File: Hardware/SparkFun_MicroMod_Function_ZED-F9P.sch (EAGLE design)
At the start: 39 parts, among them J11 MICROMOD_STANDARD, J5 QWIIC_RA, U1 EEPROM, U2 U-BLOX_ZED-F9P

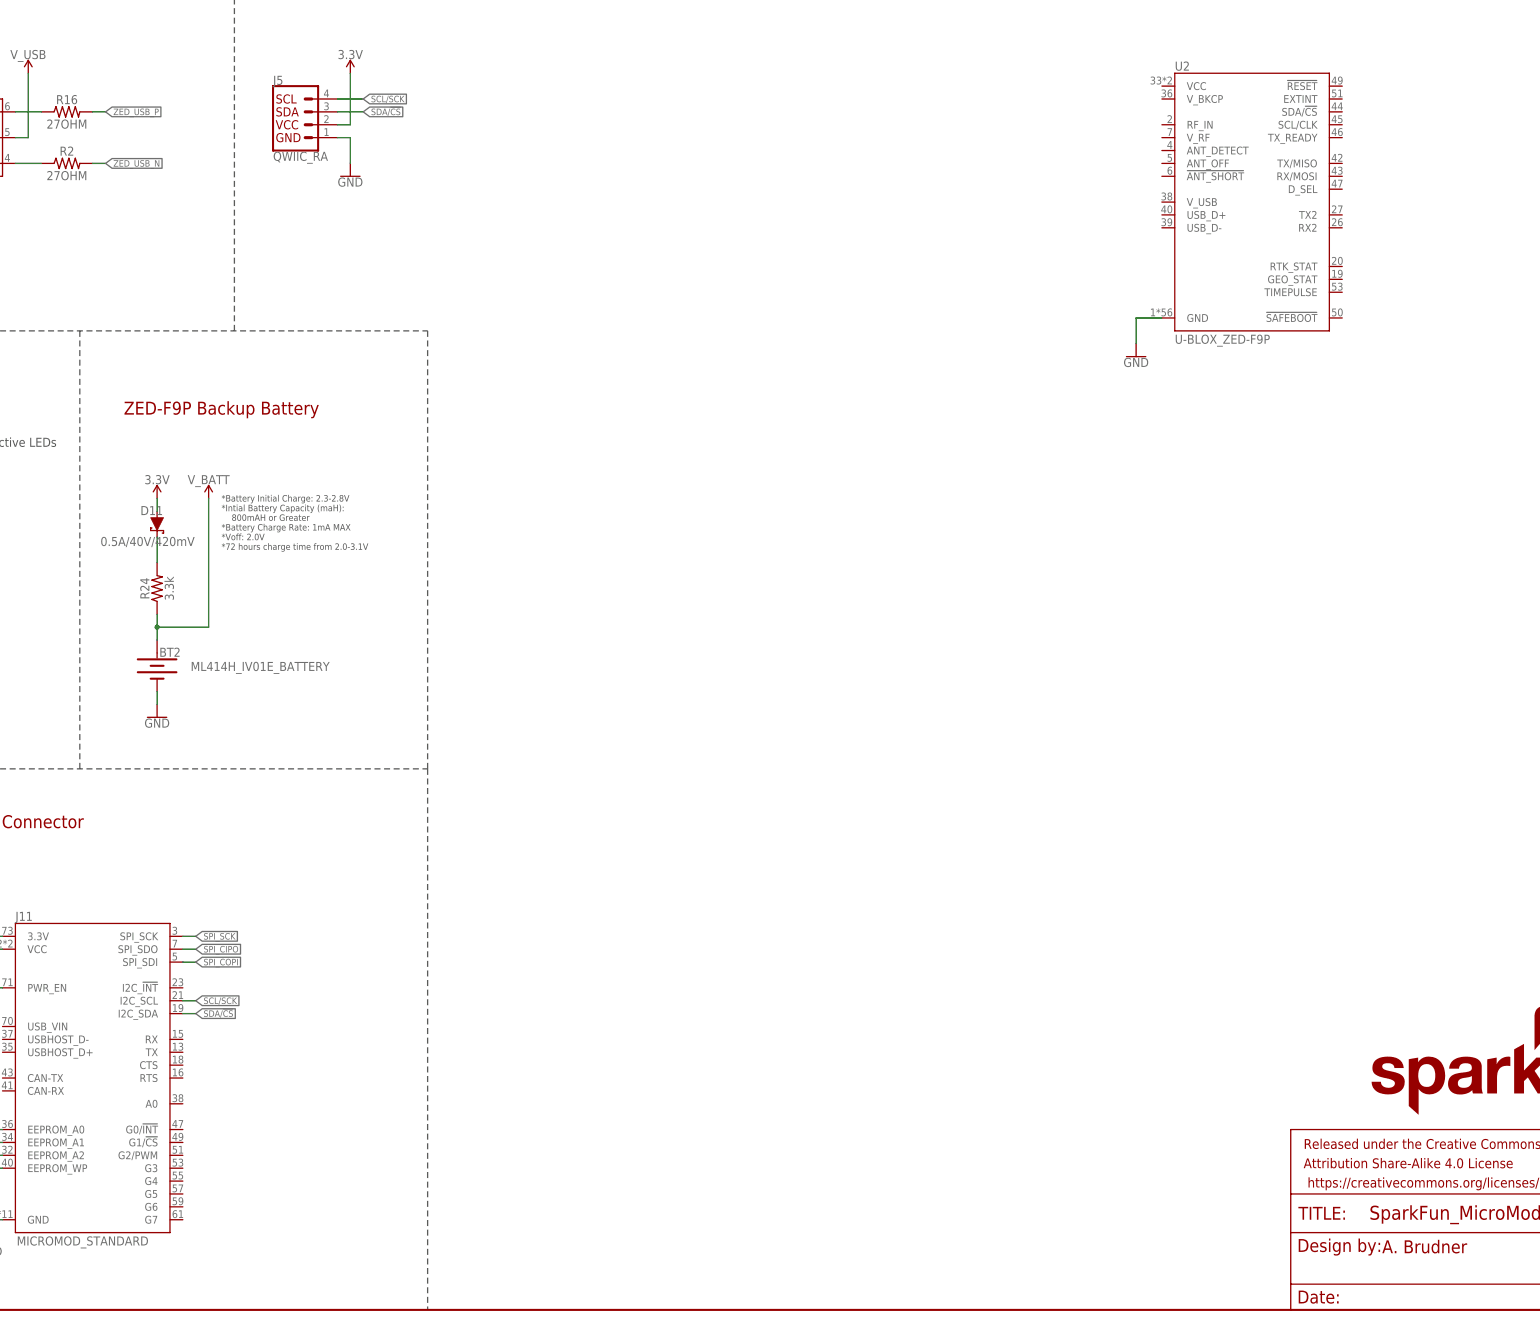
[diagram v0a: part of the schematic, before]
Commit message: Added I2C protection for ZED_F9P
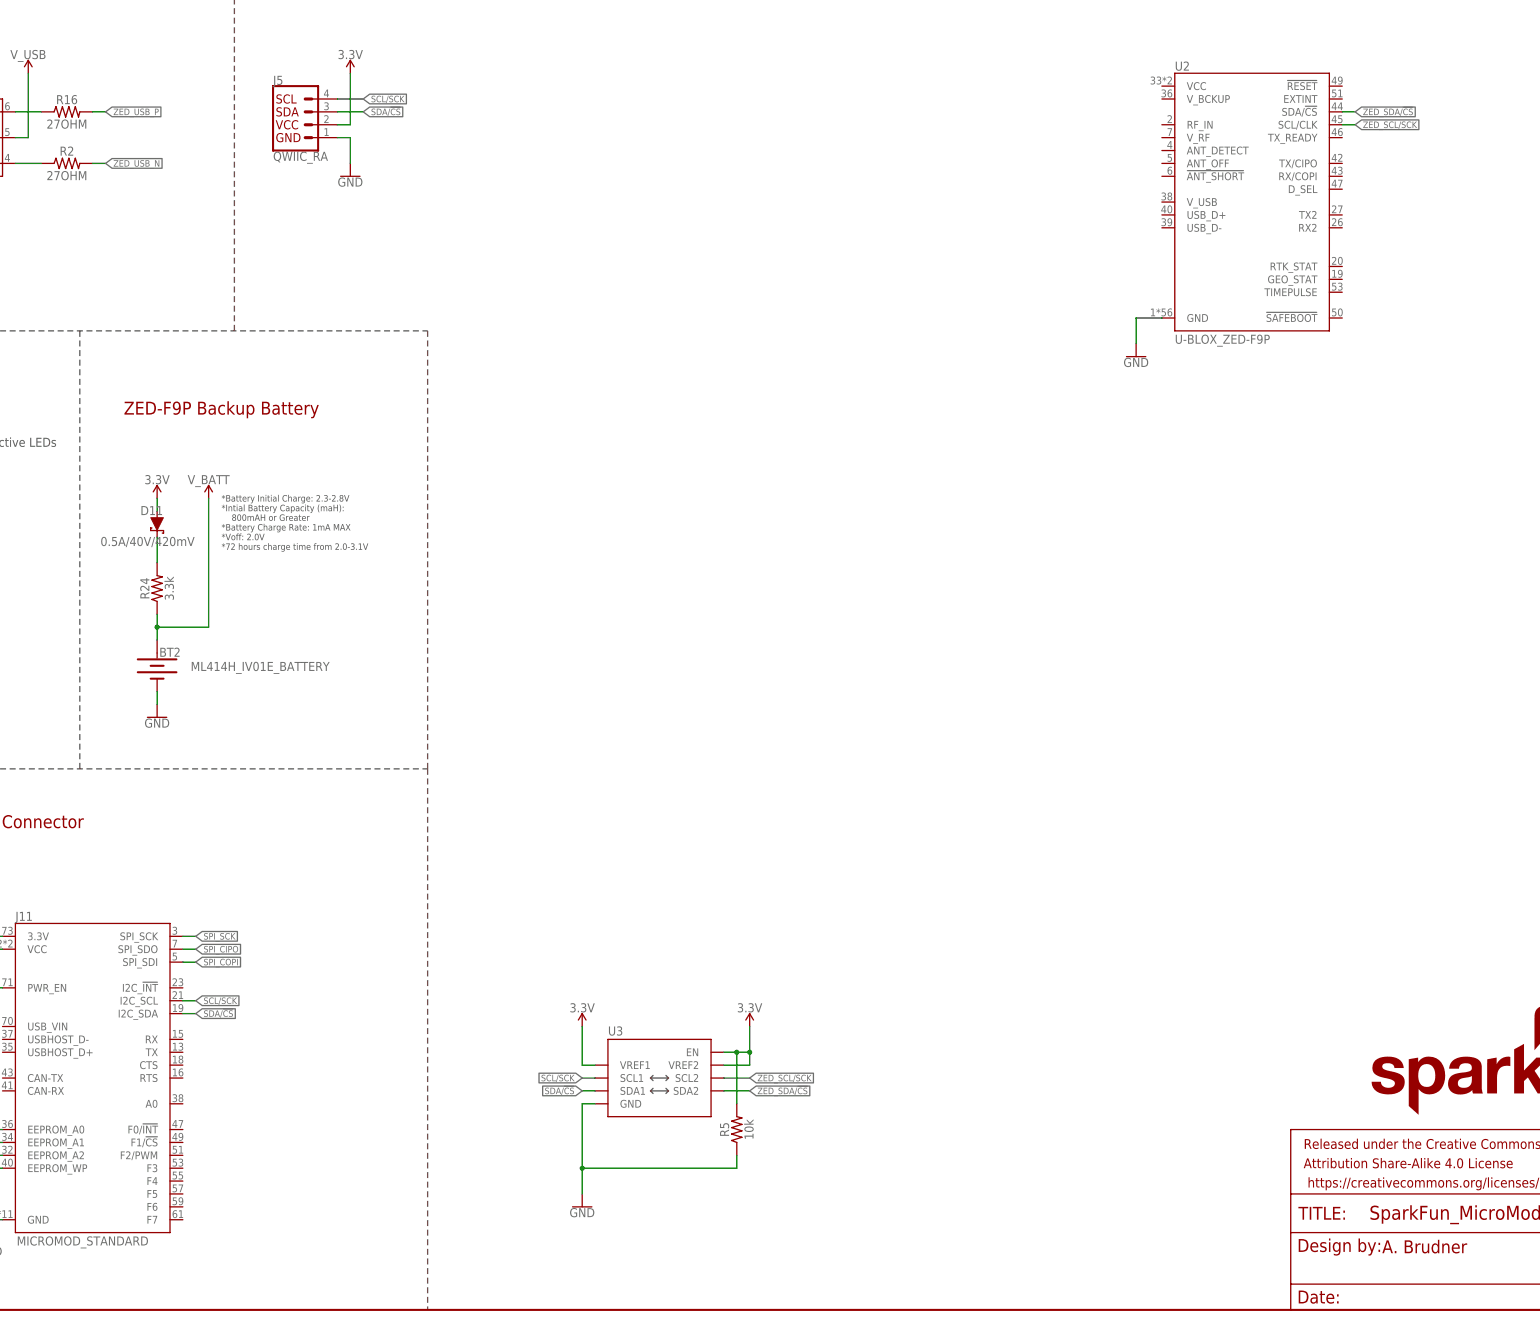
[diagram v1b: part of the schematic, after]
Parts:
- added R5: 10k, SparkFun-Resistors:10KOHM-0603-1/10W-1%
- added U3: (no value), SparkFun-IC-Comms:PCA9306VSSOP_DCU
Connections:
- new net ZED_SCL/SCK: U2.SCL/CLK, U3.SCL2
- new net ZED_SDA/!CS!: U2.SDA/!CS!, U3.SDA2
- net 3.3V: now also R5.2, U3.EN, U3.VREF1, U3.VREF2
- net GND: now also R5.1, U3.GND
- net SCL/SCK: now also U3.SCL1
- net SDA/!CS!: now also U3.SDA1
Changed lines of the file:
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@@
 <part name="GND27" library="SparkFun-PowerSymbols" deviceset="GND" device=""/>
 <part name="SUPPLY11" library="SparkFun-PowerSymbols" deviceset="3.3V" device=""/>
+<part name="U3" library="SparkFun-IC-Comms" deviceset="PCA9306" device="VSSOP_DCU" package3d_urn="urn:adsk.eagle:package:34687508/1"/>
+<part name="GND4" library="SparkFun-PowerSymbols" deviceset="GND" device=""/>
+<part name="SUPPLY10" library="SparkFun-PowerSymbols" deviceset="3.3V" device=""/>
+<part name="SUPPLY12" library="SparkFun-PowerSymbols" deviceset="3.3V" device=""/>
+<part name="R5" library="SparkFun-Resistors" deviceset="10KOHM" device="-0603-1/10W-1%" value="10k"/>
 </parts>
 <sheets>
@@
 <attribute name="VALUE" x="144.78" y="246.634" size="1.778" layer="96" font="vector" align="bottom-center"/>
 </instance>
+<instance part="U3" gate="G$1" x="205.74" y="45.72" smashed="yes">
+<attribute name="NAME" x="195.58" y="54.102" size="1.778" layer="95"/>
+<attribute name="VALUE" x="195.58" y="35.56" size="1.778" layer="96"/>
+</instance>
+<instance part="GND4" gate="1" x="190.5" y="20.32" smashed="yes">
+<attribute name="VALUE" x="190.5" y="20.066" size="1.778" layer="96" font="vector" align="top-center"/>
+</instance>
+<instance part="SUPPLY10" gate="G$1" x="190.5" y="55.88" smashed="yes">
+<attribute name="VALUE" x="190.5" y="58.674" size="1.778" layer="96" align="bottom-center"/>
+</instance>
+<instance part="SUPPLY12" gate="G$1" x="223.52" y="55.88" smashed="yes">
+<attribute name="VALUE" x="223.52" y="58.674" size="1.778" layer="96" align="bottom-center"/>
+</instance>
+<instance part="R5" gate="G$1" x="220.98" y="35.56" smashed="yes" rot="R90">
+<attribute name="NAME" x="219.456" y="35.56" size="1.778" layer="95" font="vector" rot="R90" align="bottom-center"/>
+<attribute name="VALUE" x="222.504" y="35.56" size="1.778" layer="96" font="vector" rot="R90" align="top-center"/>
+</instance>
 </instances>
 <busses>
@@
 <wire x1="142.24" y1="231.14" x2="144.78" y2="231.14" width="0.1524" layer="91"/>
 </segment>
+<segment>
+<pinref part="U3" gate="G$1" pin="GND"/>
+<wire x1="193.04" y1="40.64" x2="190.5" y2="40.64" width="0.1524" layer="91"/>
+<wire x1="190.5" y1="40.64" x2="190.5" y2="27.94" width="0.1524" layer="91"/>
+<pinref part="GND4" gate="1" pin="GND"/>
+<pinref part="R5" gate="G$1" pin="1"/>
+<wire x1="190.5" y1="27.94" x2="190.5" y2="22.86" width="0.1524" layer="91"/>
+<wire x1="190.5" y1="27.94" x2="220.98" y2="27.94" width="0.1524" layer="91"/>
+<wire x1="220.98" y1="27.94" x2="220.98" y2="30.48" width="0.1524" layer="91"/>
+<junction x="190.5" y="27.94"/>
+</segment>
 </net>
 <net name="3.3V" class="0">
@@
 <wire x1="142.24" y1="233.68" x2="144.78" y2="233.68" width="0.1524" layer="91"/>
 <pinref part="SUPPLY11" gate="G$1" pin="3.3V"/>
+</segment>
+<segment>
+<pinref part="U3" gate="G$1" pin="VREF1"/>
+<wire x1="193.04" y1="48.26" x2="190.5" y2="48.26" width="0.1524" layer="91"/>
+<wire x1="190.5" y1="48.26" x2="190.5" y2="55.88" width="0.1524" layer="91"/>
+<pinref part="SUPPLY10" gate="G$1" pin="3.3V"/>
+</segment>
+<segment>
+<pinref part="U3" gate="G$1" pin="VREF2"/>
+<wire x1="218.44" y1="48.26" x2="223.52" y2="48.26" width="0.1524" layer="91"/>
+<wire x1="223.52" y1="48.26" x2="223.52" y2="50.8" width="0.1524" layer="91"/>
+<pinref part="U3" gate="G$1" pin="EN"/>
+<wire x1="223.52" y1="50.8" x2="223.52" y2="55.88" width="0.1524" layer="91"/>
+<wire x1="218.44" y1="50.8" x2="220.98" y2="50.8" width="0.1524" layer="91"/>
+<junction x="223.52" y="50.8"/>
+<pinref part="SUPPLY12" gate="G$1" pin="3.3V"/>
+<pinref part="R5" gate="G$1" pin="2"/>
+<wire x1="220.98" y1="50.8" x2="223.52" y2="50.8" width="0.1524" layer="91"/>
+<wire x1="220.98" y1="40.64" x2="220.98" y2="50.8" width="0.1524" layer="91"/>
+<junction x="220.98" y="50.8"/>
 </segment>
 </net>
@@
 <label x="114.3" y="60.96" size="1.27" layer="95" xref="yes"/>
 </segment>
+<segment>
+<pinref part="U3" gate="G$1" pin="SCL1"/>
+<wire x1="193.04" y1="45.72" x2="190.5" y2="45.72" width="0.1524" layer="91"/>
+<label x="190.5" y="45.72" size="1.27" layer="95" rot="R180" xref="yes"/>
+</segment>
 </net>
 <net name="SDA/!CS!" class="0">
@@
 <label x="114.3" y="58.42" size="1.27" layer="95" xref="yes"/>
 </segment>
-</net>
+<segment>
+<pinref part="U3" gate="G$1" pin="SDA1"/>
+<wire x1="193.04" y1="43.18" x2="190.5" y2="43.18" width="0.1524" layer="91"/>
+<label x="190.5" y="43.18" size="1.27" layer="95" rot="R180" xref="yes"/>
+</segment>
+</net>
+<net name="ZED_SCL/SCK" class="0">
+<segment>
+<pinref part="U3" gate="G$1" pin="SCL2"/>
+<wire x1="218.44" y1="45.72" x2="223.52" y2="45.72" width="0.1524" layer="91"/>
+<label x="223.52" y="45.72" size="1.27" layer="95" xref="yes"/>
+</segment>
+<segment>
+<pinref part="U2" gate="U1" pin="SCL/CLK"/>
+<wire x1="340.36" y1="233.68" x2="342.9" y2="233.68" width="0.1524" layer="91"/>
+<label x="342.9" y="233.68" size="1.27" layer="95" xref="yes"/>
+</segment>
+</net>
+<net name="ZED_SDA/!CS!" class="0">
+<segment>
+<pinref part="U3" gate="G$1" pin="SDA2"/>
+<wire x1="218.44" y1="43.18" x2="223.52" y2="43.18" width="0.1524" layer="91"/>
+<label x="223.52" y="43.18" size="1.27" layer="95" xref="yes"/>
+</segment>
+<segment>
+<pinref part="U2" gate="U1" pin="SDA/!CS!"/>
+<wire x1="340.36" y1="236.22" x2="342.9" y2="236.22" width="0.1524" layer="91"/>
+<label x="342.9" y="236.22" size="1.27" layer="95" xref="yes"/>
+</segment>
+</net>

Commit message: Created local library. Added ZED-F9P to sch.
Created Local library.
Added inverter to lib.
Added octal buffer to lib.
Added modified ZED-F9P to lib.
Added ZED-F9P to sch.
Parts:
- removed U2: U-BLOX_ZED-F9P, SparkFun-GPS:U-BLOX_ZED-F9P
- removed U3: (no value), SparkFun-IC-Comms:PCA9306VSSOP_DCU
- renumbered BT2 to $1_0_$_2022-03-17_14-46-28, C4 to $1_1_$_2022-03-17_14-46-28, D10 to $1_6_$_2022-03-17_14-46-28, D11 to $1_8_$_2022-03-17_14-46-28, D2 to $1_3_$_2022-03-17_14-46-28, D3 to $1_2_$_2022-03-17_14-46-28, D4 to $1_7_$_2022-03-17_14-46-28, D8 to $1_4_$_2022-03-17_14-46-28, D9 to $1_5_$_2022-03-17_14-46-28, FD1 to $1_9_$_2022-03-17_14-46-28, FD2 to $1_11_$_2022-03-17_14-46-28, FD3 to $1_12_$_2022-03-17_14-46-28, FD4 to $1_10_$_2022-03-17_14-46-28, FRAME1 to $1_13_$_2022-03-17_14-46-28
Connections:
- removed net ZED_SCL/SCK: U2.SCL/CLK, U3.SCL2
- removed net ZED_SDA/!CS!: U2.SDA/!CS!, U3.SDA2
- net 3.3V: no longer U3.EN, U3.VREF1, U3.VREF2
- net GND: no longer U2.GND, U3.GND
- net SCL/SCK: no longer U3.SCL1
- net SDA/!CS!: no longer U3.SDA1

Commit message: Filled out octal buffers, labeled nets. Modified inverter sch symbol.
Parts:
- removed $1_1_$_2022-03-17_14-46-28: 0.1uF, SparkFun-Capacitors:0.1UF-0603-25V-(+80/-20%)
- removed J11: MICROMOD_STANDARD, SparkFun-MicroMod-Function:MICROMOD_STANDARD
- removed J5: QWIIC_RA, SparkFun-Connectors:QWIIC_CONNECTORJS-1MM
- removed R19, R21: 1k, SparkFun-Resistors:1KOHM-0603-1/10W-1%
- removed R22: 10k, SparkFun-Resistors:10KOHM-0603-1/10W-1%
- removed RTK: JUMPER-SMT_2_NC_TRACE_SILK, SparkFun-Jumpers:JUMPER-SMT_2_NC_TRACE_SILK
- added C1: 10pF, SparkFun-Capacitors:10PF-0603-50V-5%
- added C2: 0.1uF, SparkFun-Capacitors:0.1UF-0603-25V-(+80/-20%)
- added J1: (no value), SparkFun-Connectors:USB_C_2-LAYER_PADS
- added J2: MICROMOD_STANDARD, SparkFun-MicroMod-Function:MICROMOD_STANDARD
- added JP1: JUMPER-SMT_2_NO_SILK, SparkFun-Jumpers:JUMPER-SMT_2_NO_SILK
- added JP7: NC, SparkFun-Jumpers:JUMPER-SMT_2_NC_TRACE_SILK
- added R10, R9: 27OHM, SparkFun-Resistors:27OHM
- added R12: 220k, SparkFun-Resistors:220KOHM-0603-1/10W-1%
- added R13, R14, R15: 1.5k, SparkFun-Resistors:1.5KOHM-0603-1/10W-1%
- added R17: 10k, SparkFun-Resistors:10KOHM-0603-1/10W-1%
- added R8: 5.1k, SparkFun-Resistors:5.1KOHM5.1KOHM-0603-1/10W-1%
- added U2: PCA9306DCUR, MicroMod_Function_GNSS_ublox_ZED-F9P:PCA9306DCUR
- added U3: U-BLOX_ZED-F9P, MicroMod_Function_GNSS_ublox_ZED-F9P:U-BLOX_ZED-F9P
- added U4, U5: 74LVC541ABQ, MicroMod_Function_GNSS_ublox_ZED-F9P:74LVC541ABQ
- added U6: SN74AUP1T04DCK, MicroMod_Function_GNSS_ublox_ZED-F9P:SN74AUP1T04DCK
- J3: value (none) -> QWIIC_RA; device SparkFun-Connectors:USB_C_2-LAYER_PADS -> SparkFun-Connectors:QWIIC_CONNECTORJS-1MM
- JP5: value JUMPER-SMT_2_NO_SILK -> JUMPER-SMT_2_NC_TRACE_SILK; device SparkFun-Jumpers:JUMPER-SMT_2_NO_SILK -> SparkFun-Jumpers:JUMPER-SMT_2_NC_TRACE_SILK
- R1: value 5.1k -> 10k; device SparkFun-Resistors:5.1KOHM5.1KOHM-0603-1/10W-1% -> SparkFun-Resistors:10KOHM-0603-1/10W-1%
- R16: value 27OHM -> 1.5k; device SparkFun-Resistors:27OHM -> SparkFun-Resistors:1.5KOHM-0603-1/10W-1%
- R2: value 27OHM -> 5.1k; device SparkFun-Resistors:27OHM -> SparkFun-Resistors:5.1KOHM5.1KOHM-0603-1/10W-1%
- R5: value 10k -> 1k; device SparkFun-Resistors:10KOHM-0603-1/10W-1% -> SparkFun-Resistors:1KOHM-0603-1/10W-1%
- R7: value 5.1k -> 1k; device SparkFun-Resistors:5.1KOHM5.1KOHM-0603-1/10W-1% -> SparkFun-Resistors:1KOHM-0603-1/10W-1%
- renumbered $1_0_$_2022-03-17_14-46-28 to BT1, $1_10_$_2022-03-17_14-46-28 to FD2, $1_11_$_2022-03-17_14-46-28 to FD3, $1_12_$_2022-03-17_14-46-28 to FD4, $1_13_$_2022-03-17_14-46-28 to FRAME1, $1_2_$_2022-03-17_14-46-28 to D1, $1_3_$_2022-03-17_14-46-28 to D2, $1_4_$_2022-03-17_14-46-28 to D3, $1_5_$_2022-03-17_14-46-28 to D4, $1_6_$_2022-03-17_14-46-28 to D5, $1_7_$_2022-03-17_14-46-28 to D6, $1_8_$_2022-03-17_14-46-28 to D7, $1_9_$_2022-03-17_14-46-28 to FD1, 3V3 to JP3, GEOF to JP6, PPS to JP4, R20 to R6, R24 to R11, VIN to JP2
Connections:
- removed net SPI_CIPO: J11.SPI_SDO
- removed net SPI_COPI: J11.SPI_SDI
- removed net SPI_SCK: J11.SPI_SCK
- new net !RESET!: U4.A2
- new net !SAFEBOOT!: U4.A3
- new net !SHORT!: U4.A6
- new net ANT_DETECT: U4.A5
- new net ANT_OFF: U5.Y0
- new net EXTINT: U4.A4
- new net IO_!OE!: U4.!OE1!, U4.!OE2!, U5.!OE1!, U5.!OE2!, U6.Y
- new net N$12: C1.1, R12.1, U2.EN, U2.VREF2
- new net N$13: C2.1, U1.VCC
- new net N$14: U6.A, U6.VCC
- new net N$16: JP7.2
- new net N$18: J2.A0
- new net N$19: J2.F0/!INT!
- new net N$21: J2.F2/PWM
- new net N$22: J2.F3
- new net N$23: J2.F4
- new net N$24: JP7.1, R17.2, U4.A7
- new net N$25: J2.F5
- new net N$26: J2.F6
- new net N$30: J2.F7
- new net N$31: J2.USB_VIN
- new net N$33: J2.USBHOST_D-
- new net N$34: J2.USBHOST_D+
- new net N$35: J2.CTS
- new net N$36: J2.RTS
- new net N$37: J2.CAN-TX
- new net N$38: J2.CAN-RX
- new net N$39: U4.VCC
- new net N$42: U5.VCC
- new net N$69: U3.V_USB
- new net N$73: U3.V_RF
- new net N$74: U3.RF_IN
- new net N$77: U3.VCC
- new net RX/COPI: J2.RX, J2.SPI_SDI, U4.A1
- new net RX2/RTCM: U4.A0
- new net TIMEPULSE: U5.Y6
- new net TX/CIPO: J2.SPI_SDO, J2.TX, U5.Y4
- new net TX2/RTCM: U5.Y3
- new net TX_READY: J2.I2C_!INT!, U5.Y5
- new net ZED_!ANT_SHORT!: U3.!ANT_SHORT!
- new net ZED_!RESET!: U3.!RESET!, U4.Y2
- new net ZED_!SAFEBOOT!: U3.!SAFEBOOT!, U4.Y3
- new net ZED_!SHORT!: U4.Y6
- new net ZED_ANT_DETECT: U3.ANT_DETECT, U4.Y5
- new net ZED_ANT_OFF: U3.ANT_OFF, U5.A0
- new net ZED_DSEL: U3.D_SEL, U4.Y7
- new net ZED_EXTINT: U3.EXTINT, U4.Y4
- new net ZED_GEO_STAT: U3.GEO_STAT, U5.A1
- new net ZED_RTK_STAT: U3.RTK_STAT, U5.A2
- new net ZED_RX/COPI: U3.RX/COPI, U4.Y1
- new net ZED_RX2/RTCM: U3.RX2, U4.Y0
- new net ZED_SCL/SCK: R14.1, U2.SCL2, U3.SCL/CLK
- new net ZED_SDA/!CS!: R13.1, U2.SDA2, U3.SDA/!CS!
- new net ZED_TIMEPULSE: U3.TIMEPULSE, U5.A6
- new net ZED_TX/CIPO: U3.TX/CIPO, U5.A4
- new net ZED_TX2/RTCM: U3.TX2, U5.A3
- new net ZED_TX_READY: U3.TX_READY, U5.A5
- net 3.3V: now also J2.3.3V, J3.2, R1.1, R12.2, R13.2, R14.2, R15.2, R16.2, U2.VREF1; no longer $1_1_$_2022-03-17_14-46-28.1, J11.3.3V, J5.2, R22.1, R5.2, U1.VCC
- net A0: now also J2.EEPROM_A0; no longer J11.EEPROM_A0
- net A1: now also J2.EEPROM_A1; no longer J11.EEPROM_A1
- net A2: now also J2.EEPROM_A2; no longer J11.EEPROM_A2
- net EWP: now also J2.EEPROM_WP, JP1.2, R1.2; no longer J11.EEPROM_WP, JP5.2, R22.2
- net GEO_STAT: now also U5.Y1
- net GND: now also C1.2, C2.2, J1.GND, J1.SHLD, J2.GND, J3.1, JP1.1, R17.1, R2.1, R8.1, U2.GND, U3.GND, U4.GND, U5.A7, U5.GND, U5.Y7, U6.GND; no longer $1_1_$_2022-03-17_14-46-28.2, J11.GND, J3.GND, J5.1, R1.1, R5.1, R7.1, RTK.1
- net N$1: now also J1.D+; no longer J3.D+
- net N$10: now also R3.1; no longer R4.1
- net N$11: now also R3.2; no longer R4.2
- net N$2: now also J1.D-; no longer J3.D-
- net N$27: now also R5.1; no longer R19.1
- net N$28: now also R5.2; no longer R19.2
- net N$3: now also J1.CC2, R2.2; no longer J3.CC2, R7.2
- net N$4: now also J1.CC1, R8.2; no longer J3.CC1, R1.2
- net N$45: now also R7.1; no longer R21.1
- net N$46: now also R7.2; no longer R21.2
- net N$5: now also R9.1; no longer R16.1
- net N$6: now also R10.1; no longer R2.1
- net N$7: now also R4.2; no longer R3.2
- net N$8: now also JP5.2; no longer RTK.2
- net N$9: now also R4.1; no longer R3.1
- net PWR_EN: now also J2.PWR_EN; no longer J11.PWR_EN
- net RTK_STAT: now also U5.Y2
- net SCL/SCK: now also J2.I2C_SCL, J2.SPI_SCK, J3.4, R16.1, U2.SCL1; no longer J11.I2C_SCL, J5.4
- net SDA/!CS!: now also J2.F1/!CS!, J2.I2C_SDA, J3.3, R15.1, U2.SDA1; no longer J11.I2C_SDA, J5.3
- net VCC: now also J2.VCC; no longer J11.VCC
- net V_BATT: now also U3.V_BCKUP
- net V_USB: now also J1.VBUS; no longer J3.VBUS
- net ZED_USB_N: now also R10.2, U3.USB_D-; no longer R2.2
- net ZED_USB_P: now also R9.2, U3.USB_D+; no longer R16.2
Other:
- note added: "NC"
- note added: "Qwiic Connector"
- moved on the sheet: R16, R3, R4, R5, U1
